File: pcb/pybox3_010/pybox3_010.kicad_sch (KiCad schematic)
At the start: 8 parts, among them SW1 SW_Push, SW2 SW_Push, SW3 RotaryEncoder_Switch, U1 RP2040-ZERO

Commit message: update
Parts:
- U1: footprint RP2040-ZERO:MODULE_RP2040-ZERO -> RP2040-ZERO:MODULE_RP2040-ZERO_reduced; symbol RP2040-ZERO:RP2040-ZERO -> RP2040-ZERO:RP2040-ZERO_reduced
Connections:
- no-connect marks 12 -> 7
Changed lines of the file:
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@@
-	)
-	(no_connect
-		(at 144.78 73.66)
 	)
 	(no_connect
@@
 	)
 	(no_connect
-		(at 144.78 71.12)
-	)
-	(no_connect
 		(at 109.22 78.74)
-	)
-	(no_connect
-		(at 144.78 68.58)
-	)
-	(no_connect
-		(at 109.22 88.9)
-	)
-	(no_connect
-		(at 144.78 66.04)
 	)
 	(no_connect
@@
 	)
 	(symbol
-		(lib_id "RP2040-ZERO:RP2040-ZERO")
+		(lib_id "RP2040-ZERO:RP2040-ZERO_reduced")
 		(at 127 76.2 0)
 		(unit 1)
@@
 			)
 		)
-		(property "Footprint" "RP2040-ZERO:MODULE_RP2040-ZERO"
+		(property "Footprint" "RP2040-ZERO:MODULE_RP2040-ZERO_reduced"
 			(at 127 76.2 0)
 			(effects
@@
 		(pin "20"
 		)
-		(pin "14"
-		)
 		(pin "16"
 		)
@@
 		(pin "19"
 		)
-		(pin "13"
-		)
 		(pin "3"
 		)
@@
 		(pin "15"
 		)
-		(pin "11"
-		)
 		(pin "7"
 		)
 		(pin "8"
 		)
-		(pin "12"
-		)
 		(pin "9"
 		)
-		(pin "10"
-		)
 		(instances

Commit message: update
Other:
- note added: "ERRORE: i pot vanno alimentati con 3V3!!!"
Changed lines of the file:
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@@
 (kicad_sch
-	(version 20231120)
+	(version 20250114)
 	(generator "eeschema")
-	(generator_version "8.0")
+	(generator_version "9.0")
 	(paper "A4")
+	(text "ERRORE: i pot vanno alimentati con 3V3!!!"
+		(exclude_from_sim no)
+		(at 152.908 47.244 0)
+		(effects
+			(font
+				(size 1.27 1.27)
+			)
+		)
+	)
 	(no_connect
 		(at 144.78 88.9)
@@
 		)
 	)
+	(embedded_fonts no)
 )

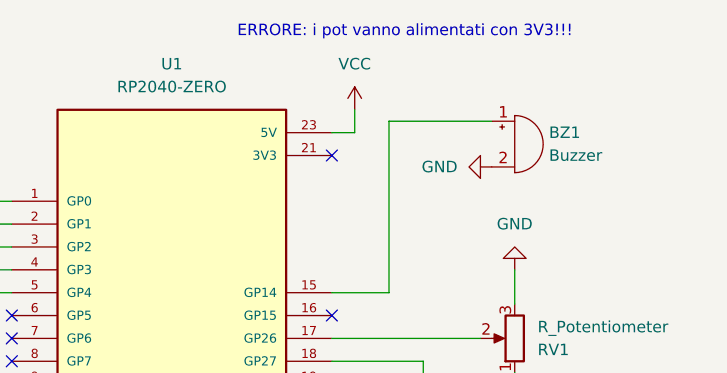
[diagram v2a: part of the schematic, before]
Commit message: FIXED: substituted 5V with 3V3 power pin
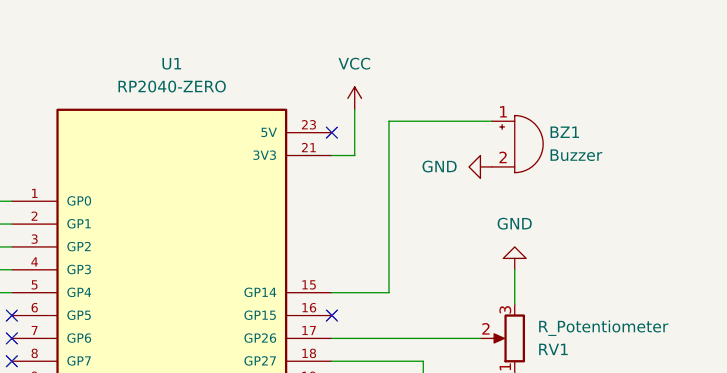
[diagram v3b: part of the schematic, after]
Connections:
- net VCC: now also U1.21 (3V3); no longer U1.23 (5V)
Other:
- note removed: "ERRORE: i pot vanno alimentati con 3V3!!!"
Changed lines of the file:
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@@
 	(generator_version "9.0")
 	(paper "A4")
-	(text "ERRORE: i pot vanno alimentati con 3V3!!!"
-		(exclude_from_sim no)
-		(at 152.908 47.244 0)
-		(effects
-			(font
-				(size 1.27 1.27)
-			)
-		)
-	)
 	(no_connect
 		(at 144.78 88.9)
 	)
 	(no_connect
-		(at 144.78 60.96)
-	)
-	(no_connect
 		(at 109.22 83.82)
 	)
@@
 	)
 	(no_connect
+		(at 144.78 58.42)
+	)
+	(no_connect
 		(at 144.78 78.74)
 	)
@@
 	(wire
 		(pts
-			(xy 144.78 58.42) (xy 147.32 58.42)
-		)
-		(stroke
-			(width 0)
-			(type default)
-		)
-	)
-	(wire
-		(pts
 			(xy 96.52 78.74) (xy 96.52 68.58)
 		)
@@
 	(wire
 		(pts
-			(xy 147.32 58.42) (xy 147.32 55.88)
-		)
-		(stroke
+			(xy 147.32 55.88) (xy 147.32 60.96)
+		)
+		(stroke
+			(width 0)
+			(type default)
+		)
+	)
+	(wire
+		(pts
+			(xy 144.78 60.96) (xy 147.32 60.96)
+		)
+		(stroke
